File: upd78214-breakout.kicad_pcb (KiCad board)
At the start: 2 copper layers, 80 x 71 mm, 31 parts, among them J1 Conn_02x17_Odd_Even, U1 upd78214-64p-qfp, X1 USB-B1HSB6

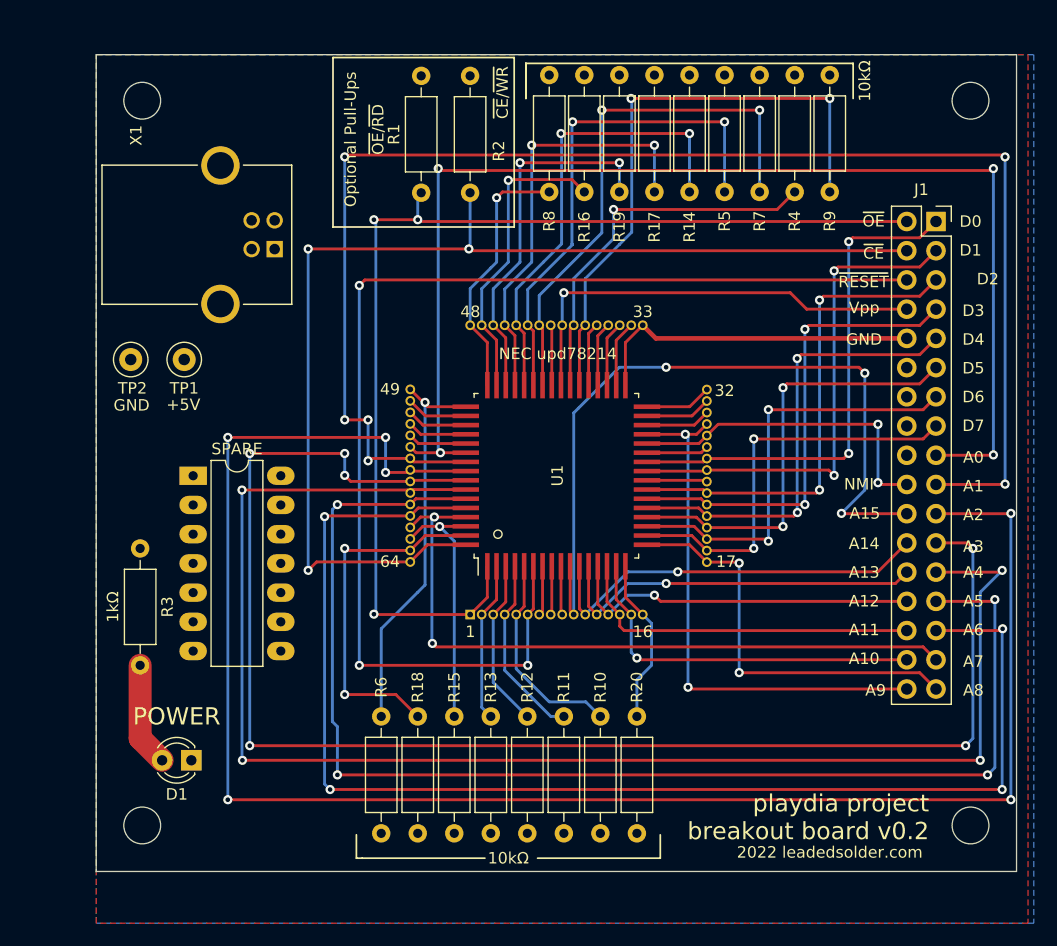
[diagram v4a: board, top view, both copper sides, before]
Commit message: 12V injection hooks
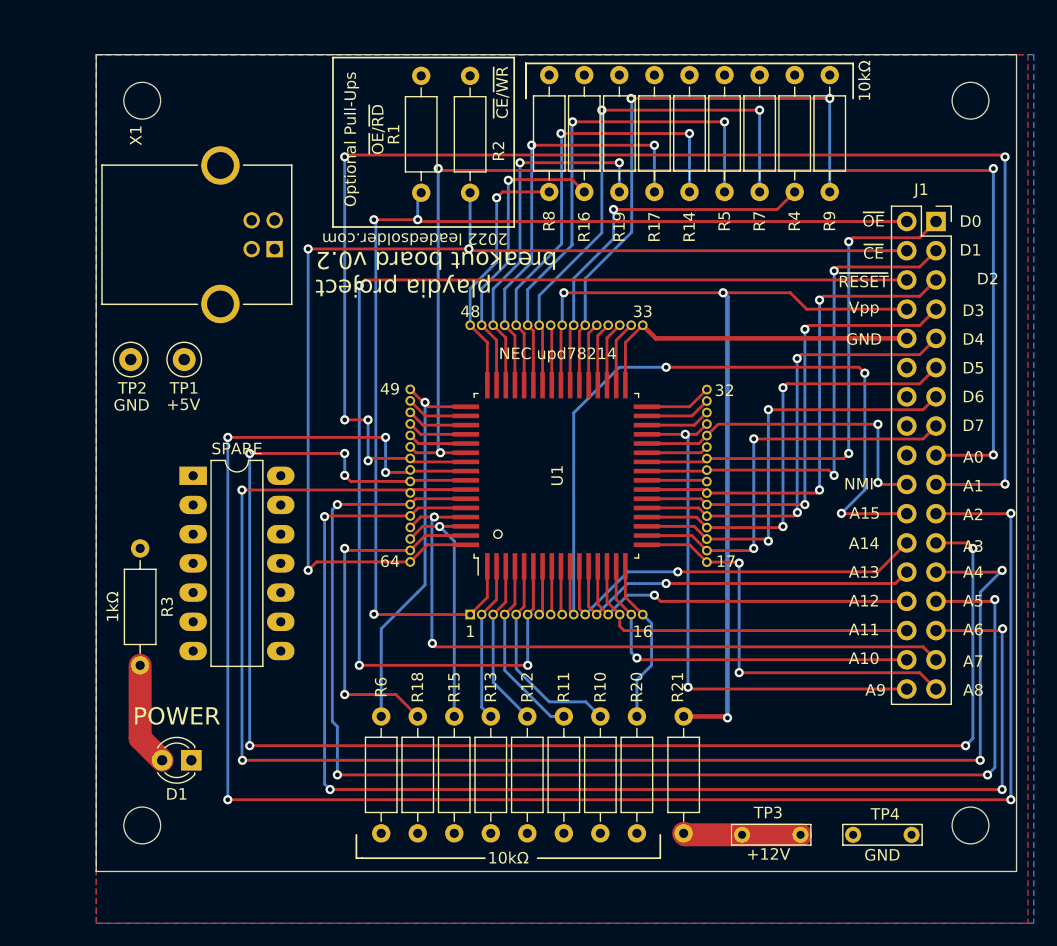
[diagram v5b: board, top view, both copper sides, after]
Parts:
- added R21: 10kΩ, Resistor_THT:R_Axial_DIN0207_L6.3mm_D2.5mm_P10.16mm_Horizontal, F.Cu at (131.1, 146.7)
- added TP3: +12V, TestPoint:TestPoint_Bridge_Pitch5.08mm_Drill0.7mm, F.Cu at (141.2, 146.8)
- added TP4: GND, TestPoint:TestPoint_Bridge_Pitch5.08mm_Drill0.7mm, F.Cu at (145.8, 146.8)
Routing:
- net /PROG_Vpp: track 38.5 -> 79.5 mm, vias 1 -> 3
- net +12V: track 0.00 -> 10.2 mm

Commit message: V2 released
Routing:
- net GND: track 71.6 -> 83.1 mm, vias 0 -> 2
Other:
- board text added: "apply +12V to pull up Vpp"
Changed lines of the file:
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@@
       (drillshape 0)
       (scaleselection 1)
-      (outputdirectory "upd78214-dumper-v1")
+      (outputdirectory "upd78214-dumper-v2")
     )
   )
@@
   (gr_line (start 117.348 79.756) (end 145.796 79.756) (layer "F.SilkS") (width 0.15))
   (gr_rect (start 116.332 79.248) (end 100.584 93.98) (layer "F.SilkS") (width 0.15) (fill none))
-  (gr_line (start 118.364 148.844) (end 129.032 148.844) (layer "F.SilkS") (width 0.15))
+  (gr_line (start 118.364 148.844) (end 133.096 148.844) (layer "F.SilkS") (width 0.15))
   (gr_line (start 145.796 79.756) (end 145.796 82.804) (layer "F.SilkS") (width 0.15))
   (gr_line (start 103.124 148.844) (end 102.616 148.844) (layer "F.SilkS") (width 0.15))
   (gr_line (start 102.616 148.844) (end 102.616 146.812) (layer "F.SilkS") (width 0.15))
   (gr_line (start 117.348 79.756) (end 117.348 82.804) (layer "F.SilkS") (width 0.15))
-  (gr_line (start 129.032 148.844) (end 129.032 146.812) (layer "F.SilkS") (width 0.15))
+  (gr_line (start 133.096 148.844) (end 133.096 146.812) (layer "F.SilkS") (width 0.15))
   (gr_poly
     (pts
@@
   )
   (gr_text "16" (at 127.508 129.159) (layer "F.SilkS")
+    (effects (font (size 1 1) (thickness 0.15)))
+  )
+  (gr_text "apply +12V to pull up Vpp" (at 145.288 141.478) (layer "F.SilkS")
     (effects (font (size 1 1) (thickness 0.15)))
   )
@@
   (segment (start 127.874 109.6) (end 131.588 109.6) (width 0.25) (layer "F.Cu") (net 51))
   (segment (start 127.874 116) (end 132.974 116) (width 0.25) (layer "F.Cu") (net 51))
+  (segment (start 127.874 111.2) (end 124.916 111.2) (width 0.25) (layer "F.Cu") (net 51))
   (segment (start 119.6 127.572) (end 119.507 127.665) (width 0.25) (layer "F.Cu") (net 51))
   (segment (start 132.974 116) (end 133.081 116.107) (width 0.25) (layer "F.Cu") (net 51))
+  (segment (start 124.919 116) (end 127.874 116) (width 0.25) (layer "F.Cu") (net 51))
+  (segment (start 124.916 111.2) (end 124.714 110.998) (width 0.25) (layer "F.Cu") (net 51))
   (segment (start 126 104.026) (end 127.507 102.519) (width 0.25) (layer "F.Cu") (net 51))
   (segment (start 128.648 103.66) (end 127.507 102.519) (width 0.4) (layer "F.Cu") (net 51))
@@
   (segment (start 131.588 109.6) (end 133.081 108.107) (width 0.25) (layer "F.Cu") (net 51))
   (segment (start 150.46 103.66) (end 128.648 103.66) (width 0.4) (layer "F.Cu") (net 51))
+  (segment (start 124.841 116.078) (end 124.919 116) (width 0.25) (layer "F.Cu") (net 51))
   (segment (start 126 107.726) (end 126 104.026) (width 0.25) (layer "F.Cu") (net 51))
   (segment (start 125.2 107.726) (end 125.2 103.826) (width 0.25) (layer "F.Cu") (net 51))
@@
   (segment (start 120.4 127.558) (end 120.507 127.665) (width 0.25) (layer "F.Cu") (net 51))
   (segment (start 125.2 103.826) (end 126.507 102.519) (width 0.25) (layer "F.Cu") (net 51))
+  (via (at 124.841 116.078) (size 0.8) (drill 0.4) (layers "F.Cu" "B.Cu") (net 51))
+  (via (at 124.714 110.998) (size 0.8) (drill 0.4) (layers "F.Cu" "B.Cu") (net 51))
+  (segment (start 124.714 115.951) (end 124.841 116.078) (width 0.25) (layer "B.Cu") (net 51))
+  (segment (start 124.714 110.998) (end 124.714 115.951) (width 0.25) (layer "B.Cu") (net 51))
   (segment (start 119.6 102.612) (end 119.507 102.519) (width 0.25) (layer "F.Cu") (net 52))
   (segment (start 119.6 107.726) (end 119.6 102.612) (width 0.25) (layer "F.Cu") (net 52))
